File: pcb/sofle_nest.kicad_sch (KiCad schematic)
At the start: 110 parts, among them J1 MJ-4PP-9, J2 Pheonix-1332645, J3 Conn_01x04, J4 FFC2B35-12-G_REVA2, SW1 SW_PUSH, SW10 SW_PUSH, SW11 SW_PUSH, SW12 SW_PUSH, SW13 SW_PUSH, SW14 SW_PUSH, SW15 SW_PUSH, SW16 SW_PUSH, SW17 SW_PUSH, SW18 SW_PUSH, SW19 SW_PUSH, SW2 SW_PUSH, SW20 SW_PUSH, SW21 SW_PUSH, SW22 SW_PUSH, SW23 SW_PUSH, SW24 SW_PUSH, SW25 Rotary_Encoder_Switch-Device, SW26 SW_PUSH, SW27 SW_PUSH, SW28 SW_PUSH, SW29 SW_PUSH, SW3 SW_PUSH, SW30 SW_PUSH, SW4 SW_PUSH, SW5 SW_PUSH, SW6 SW_PUSH, SW7 SW_PUSH, SW8 SW_PUSH, SW9 SW_PUSH, U2 kb2040

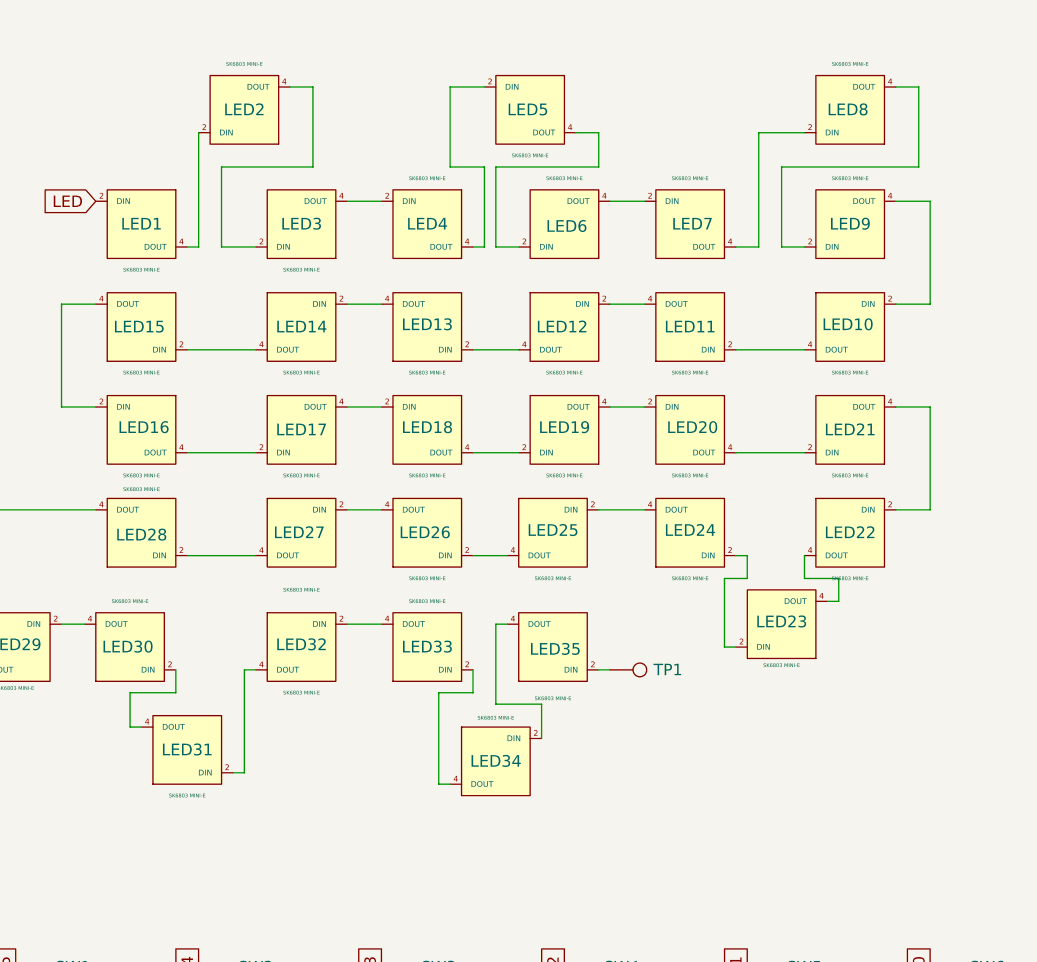
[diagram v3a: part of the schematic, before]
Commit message: Rework LED footprints to have built in vias to simplify routing
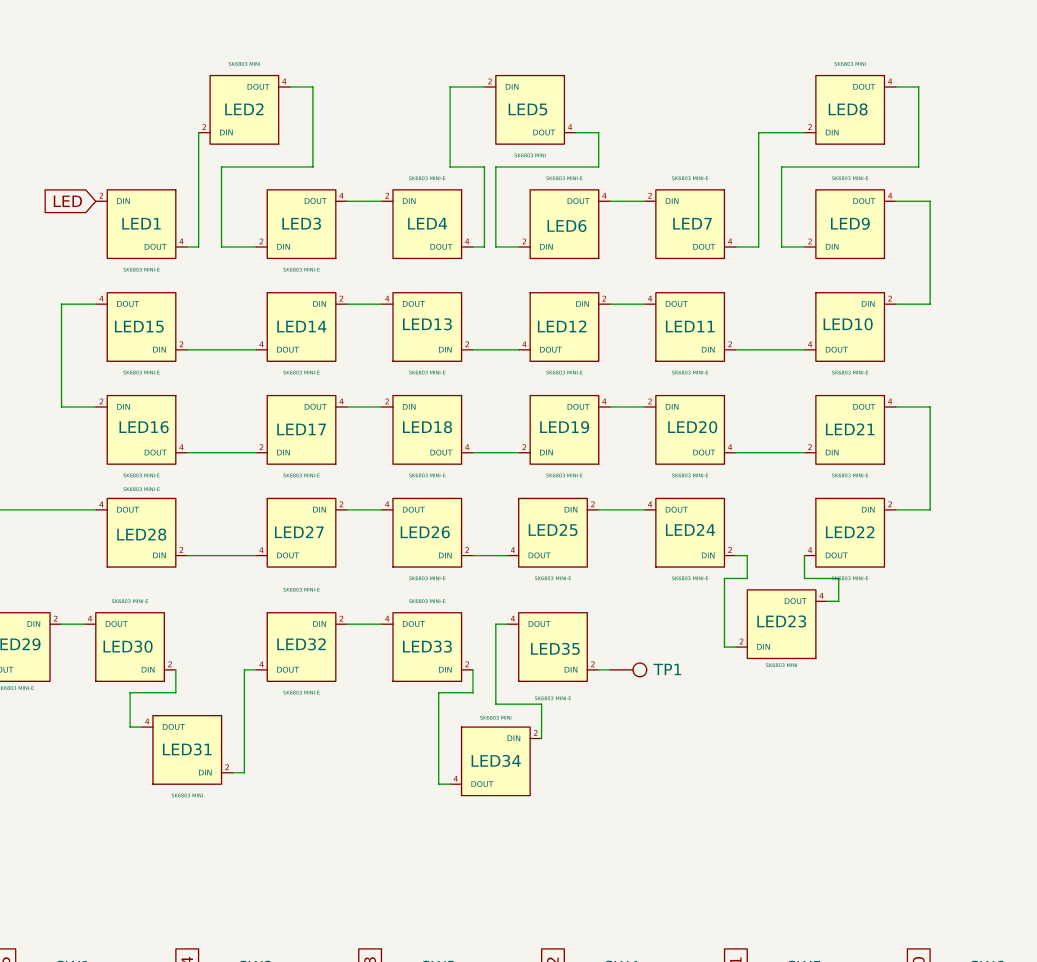
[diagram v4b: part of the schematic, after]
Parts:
- LED1, LED10, LED11, LED12, LED13, LED14, LED15, LED16, LED17, LED18, LED19, LED20, LED21, LED22, LED24, LED25, LED26, LED27, LED28, LED29, LED3, LED30, LED32, LED33, LED35, LED4, LED6, LED7, LED9: footprint Sofle_Nest:SK6803_MINI-E_v3.5.5 -> Sofle_Nest:SK6812_MINI-E; symbol Sofle_Nest:SK6803MINIE_V2 -> Sofle_Nest:SK6812-MINI-E
- LED2: value SK6803 MINI-E -> SK6803 MINI; footprint Sofle_Nest:SK6803_MINI-E_v3.5.5_Underglow -> Sofle_Nest:SK6812_MINI-E; symbol Sofle_Nest:SK6803MINIE_V2_Underglow -> Sofle_Nest:SK6812-MINI
- LED23, LED31, LED34, LED5, LED8: value SK6803 MINI-E -> SK6803 MINI; footprint Sofle_Nest:SK6803_MINI-E_v3.5.5_Underglow -> Sofle_Nest:SK6812_MINI; symbol Sofle_Nest:SK6803MINIE_V2_Underglow -> Sofle_Nest:SK6812-MINI

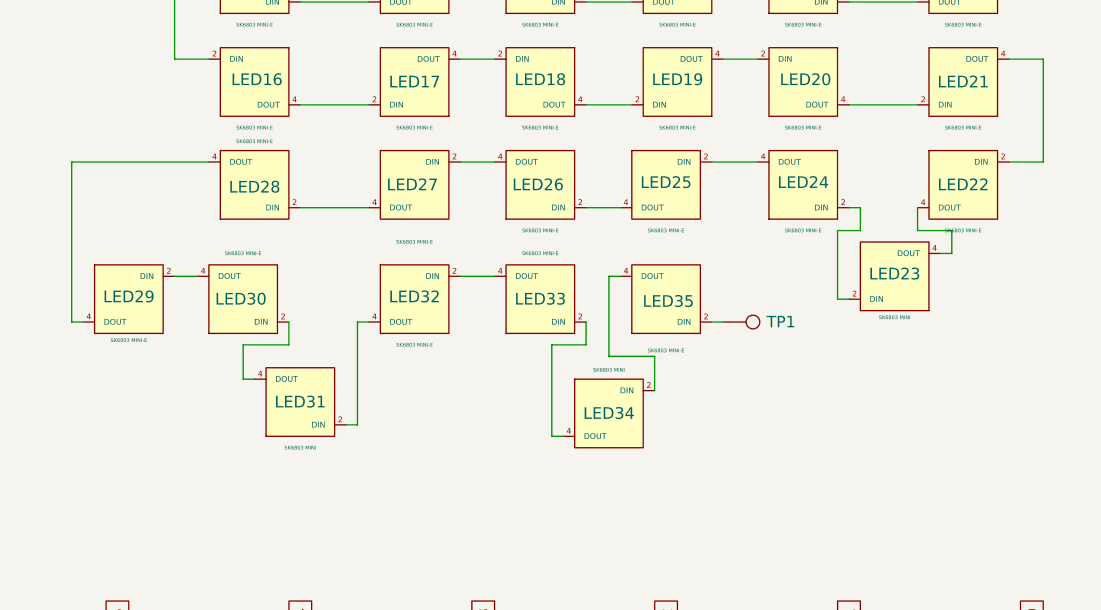
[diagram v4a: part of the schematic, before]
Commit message: Fix silk screening to be more consistent across components
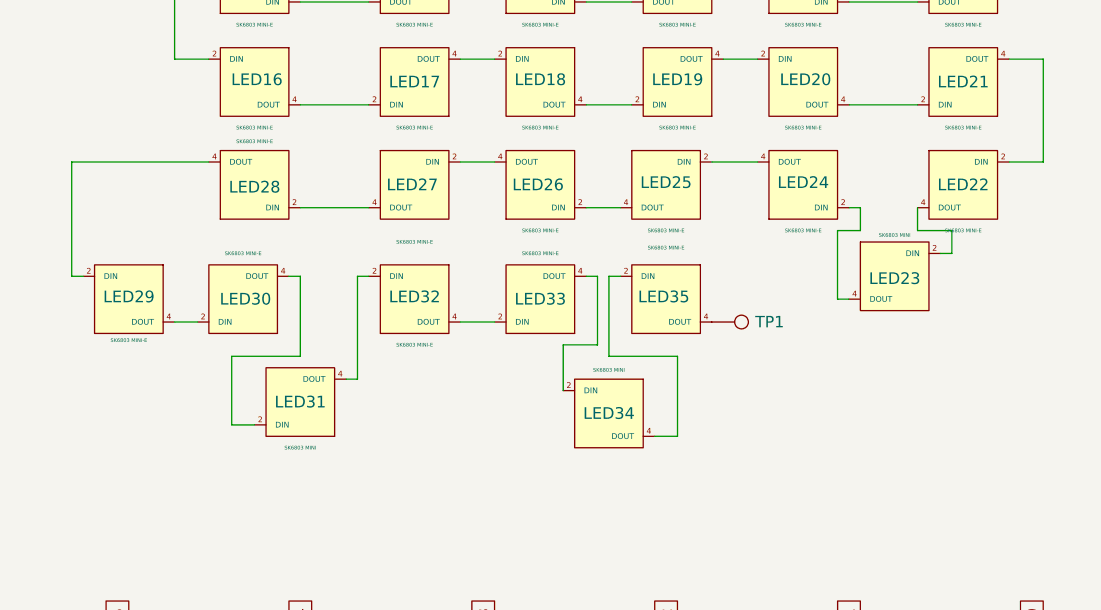
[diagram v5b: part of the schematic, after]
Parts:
- LED2: footprint Sofle_Nest:SK6812_MINI-E -> Sofle_Nest:SK6812_MINI
- SW1: footprint Sofle_Nest:Cherry_MX_DS_Hotswap_v3.5.4_SW1 -> Sofle_Nest:Cherry_MX_DS_Hotswap_v3.5.4
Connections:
- net at LED22.4 (DOUT): now also LED23.2 (DIN); no longer LED23.4 (DOUT)
- net at LED30.2 (DIN): now also LED29.4 (DOUT); no longer LED31.4 (DOUT)
- net at LED30.4 (DOUT): now also LED31.2 (DIN); no longer LED29.2 (DIN)
- net at LED32.4 (DOUT): now also LED33.2 (DIN); no longer LED31.2 (DIN)
- net at LED28.4 (DOUT): now also LED29.2 (DIN); no longer LED29.4 (DOUT)
- net at LED24.2 (DIN): now also LED23.4 (DOUT); no longer LED23.2 (DIN)
- net at LED34.4 (DOUT): now also LED35.2 (DIN); no longer LED33.2 (DIN)
- net at LED32.2 (DIN): now also LED31.4 (DOUT); no longer LED33.4 (DOUT)
- net at LED34.2 (DIN): now also LED33.4 (DOUT); no longer LED35.4 (DOUT)
- net at TP1.1: now also LED35.4 (DOUT); no longer LED35.2 (DIN)
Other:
- moved on the sheet: LED23, LED30, LED31, LED33, TP1
